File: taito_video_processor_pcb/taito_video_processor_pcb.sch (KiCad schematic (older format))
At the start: 342 parts, among them J1 14pin, J19 2pin, J2 14pin, J3 50pin, J6 50pin, Q1 2N3904, Q2 2N3904, Q3 2N3904, Q4 2N3904, Q5 2N3904, Q6 2N3904, Q7 2N3904, Q8 2N3905, SW1 SW_Push, U1 245_1, U10 4116, U100 LS00, U101 LS08, U102 LS10, U103 LS00, U104 157_1, U105 299_1, U106 299_1, U107 299_1, U108 299_1, U109 299_1, U11 4116, U110 299_1, U12 4116, U13 4116, U14 4116, U15 4116, U16 4116, U17 4116, U18 68A45, U19 86_2, U2 245_1, U20 86_1, U21 157_1, U22 LS32, U23 161_1, U24 LS04, U25 374_1, U26 4116, U27 4116, U28 4116, U29 4116, U3 2114, U30 4116, U31 4116, U32 4116, U33 4116, U34 LS374, U35 153_1, U36 LS74, U37 LS08, U38 74S113, U39 LS04, U4 2114, U40 7417, U41 4116, U42 4116, U43 4116, U44 4116, U45 4116, U46 4116, U47 4116, U48 4116, U49 LS32, U5 157_1, U50 86_3, U51 LS86, U52 153_1, U53 153_1, U54 153_1, U55 157_1, U56 2148_1, U57 2148_2, U58 7417, U59 4116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

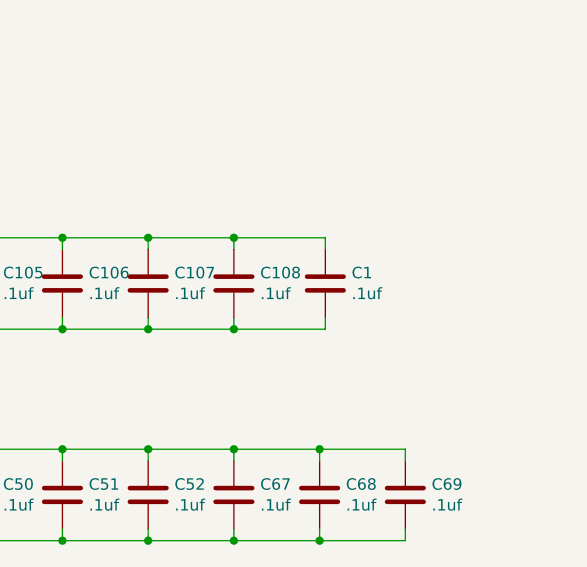
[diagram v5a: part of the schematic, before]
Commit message: PCB layout complete
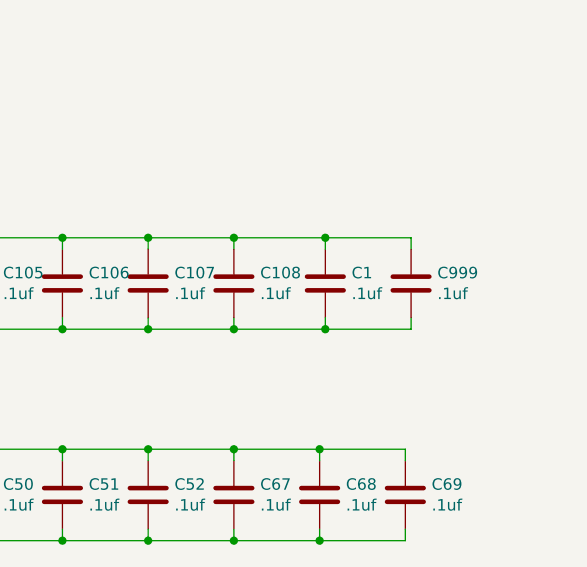
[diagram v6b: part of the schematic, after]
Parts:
- added C999: .1uf, taito_video_processor_pcb:GenericComp, symbol Device:C
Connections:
- net +5V: now also C999.1
- net GND: now also C999.2
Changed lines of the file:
@@
 Wire Wire Line
 	13150 2400 12825 2400
+$Comp
+L Device:C C999
+U 1 1 620CC81A
+P 32000 17025
+F 0 "C999" H 32115 17071 50  0000 L CNN
+F 1 ".1uf" H 32115 16980 50  0000 L CNN
+F 2 "taito_video_processor_pcb:GenericComp" H 32038 16875 50  0001 C CNN
+F 3 "~" H 32000 17025 50  0001 C CNN
+	1    32000 17025
+	1    0    0    -1
+$EndComp
+Wire Wire Line
+	32000 16875 32000 16825
+Wire Wire Line
+	32000 16825 31625 16825
+Connection ~ 31625 16825
+Wire Wire Line
+	31625 17225 32000 17225
+Wire Wire Line
+	32000 17225 32000 17175
+Connection ~ 31625 17225
 $EndSCHEMATC
